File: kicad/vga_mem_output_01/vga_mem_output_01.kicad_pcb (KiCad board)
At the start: 2 copper layers, 51.3 x 26.4 mm, 18 parts, among them J1 Conn_01x03_Socket, J2 Conn_01x02_Socket, J3 Conn_01x08_Socket, U1 74LS08, U2 74LS08

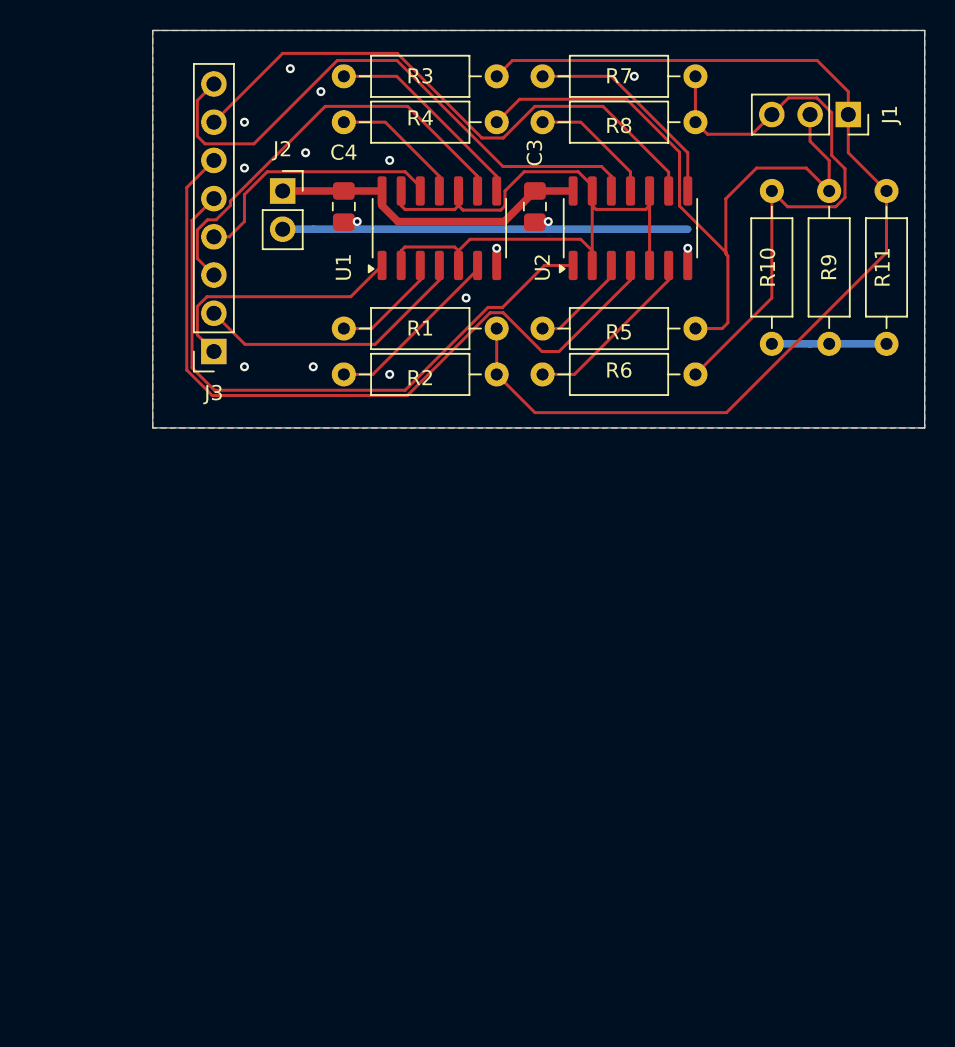
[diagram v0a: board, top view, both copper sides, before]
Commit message: more routing on 2 layer version (abandon for 4 layer version)
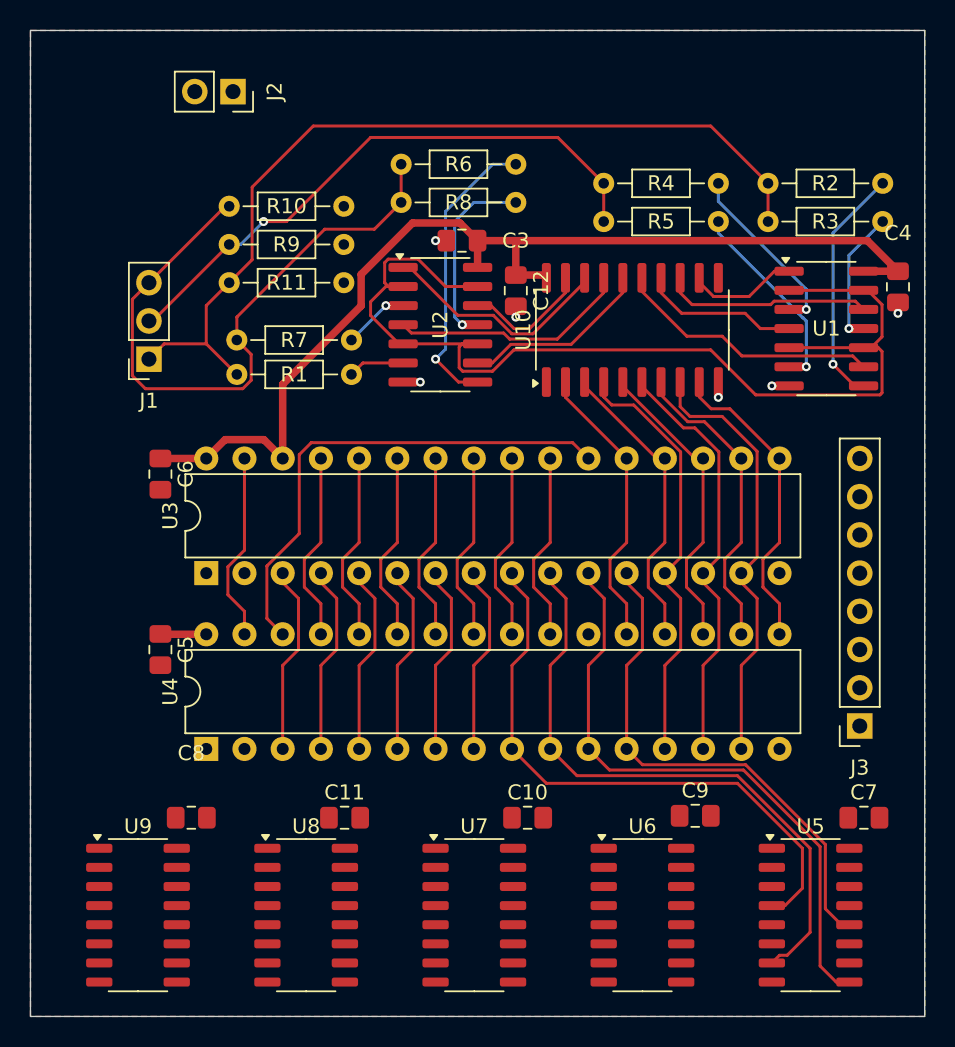
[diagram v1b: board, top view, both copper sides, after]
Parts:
- added C10: 100nF, Capacitor_SMD:C_0805_2012Metric_Pad1.18x1.45mm_HandSolder, F.Cu at (98.6, 95.0)
- added C11: 100nF, Capacitor_SMD:C_0805_2012Metric_Pad1.18x1.45mm_HandSolder, F.Cu at (86.4, 95.0)
- added C12: 100nF, Capacitor_SMD:C_0805_2012Metric_Pad1.18x1.45mm_HandSolder, F.Cu at (97.8, 60.0)
- added C5: 100nF, Capacitor_SMD:C_0805_2012Metric_Pad1.18x1.45mm_HandSolder, F.Cu at (74.2, 83.8)
- added C6: 100nF, Capacitor_SMD:C_0805_2012Metric_Pad1.18x1.45mm_HandSolder, F.Cu at (74.2, 72.2)
- added C7: 100nF, Capacitor_SMD:C_0805_2012Metric_Pad1.18x1.45mm_HandSolder, F.Cu at (120.9, 95.0)
- added C8: 100nF, Capacitor_SMD:C_0805_2012Metric_Pad1.18x1.45mm_HandSolder, F.Cu at (76.2, 95.0)
- added C9: 100nF, Capacitor_SMD:C_0805_2012Metric_Pad1.18x1.45mm_HandSolder, F.Cu at (109.7, 94.9)
- added U10: 74HCT574, Package_SO:SO-20_5.3x12.6mm_P1.27mm, F.Cu at (105.5, 62.6)
- added U3: UM61512, Package_DIP:DIP-32_W7.62mm, F.Cu at (77.2, 78.7)
- added U4: UM61512, Package_DIP:DIP-32_W7.62mm, F.Cu at (77.2, 90.4)
- added U5: 74LS157, Package_SO:SO-16_3.9x9.9mm_P1.27mm, F.Cu at (117.4, 101.5)
- added U6: 74LS157, Package_SO:SO-16_3.9x9.9mm_P1.27mm, F.Cu at (106.2, 101.5)
- added U7: 74LS157, Package_SO:SO-16_3.9x9.9mm_P1.27mm, F.Cu at (95.0, 101.5)
- added U8: 74LS157, Package_SO:SO-16_3.9x9.9mm_P1.27mm, F.Cu at (83.9, 101.5)
- added U9: 74LS157, Package_SO:SO-16_3.9x9.9mm_P1.27mm, F.Cu at (72.7, 101.5)
- R1, R10, R11, R2, R3, R4, R5, R6, R7, R8, R9: footprint Resistor_THT:R_Axial_DIN0207_L6.3mm_D2.5mm_P10.16mm_Horizontal -> Resistor_THT:R_Axial_DIN0204_L3.6mm_D1.6mm_P7.62mm_Horizontal
- moved J3 49.6 mm to (120.7, 88.9)
- moved J1 49.2 mm to (73.4, 64.5), turned to 180 degrees
- moved R2 38.0 mm to (122.2, 52.8), turned to 180 degrees
- moved C4 37.2 mm to (123.2, 59.7)
- moved R3 37.1 mm to (122.2, 55.4), turned to 180 degrees
- moved R11 36.3 mm to (86.4, 59.4), turned to 180 degrees
- moved R9 32.9 mm to (86.4, 56.9), turned to 180 degrees
- moved R10 29.9 mm to (86.4, 54.4), turned to 180 degrees
- moved U1 26.6 mm to (118.4, 62.5), turned to 0 degrees
- moved R4 25.2 mm to (111.3, 52.8), turned to 180 degrees
- moved R7 21.6 mm to (86.9, 63.2), turned to 180 degrees
- moved U2 14.2 mm to (92.8, 62.2), turned to 0 degrees
- moved R6 14.1 mm to (97.8, 51.6), turned to 180 degrees
- moved R5 13.7 mm to (111.3, 55.4), turned to 180 degrees
- moved J2 7.38 mm to (79.0, 46.7), turned to -90 degrees
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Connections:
- U1 pad 1: /PD_0 -> /PDB_3
- U1 pad 11: Net-(R4-Pad1) -> Net-(R3-Pad1)
- U1 pad 12: /PD_3 -> /PDB_2
- U1 pad 3: Net-(R1-Pad1) -> Net-(R4-Pad1)
- U1 pad 4: /PD_1 -> /PDB_4
- U1 pad 6: Net-(R2-Pad1) -> Net-(R5-Pad1)
- U1 pad 8: Net-(R3-Pad1) -> Net-(R2-Pad1)
- U1 pad 9: /PD_2 -> /PDB_1
- U2 pad 1: /PD_4 -> /PDB_6
- U2 pad 12: /PD_7 -> /PDB_7
- U2 pad 3: Net-(R5-Pad1) -> Net-(R7-Pad1)
- U2 pad 4: /PD_5 -> /PDB_0
- U2 pad 6: Net-(R6-Pad1) -> Net-(R1-Pad1)
- U2 pad 8: Net-(R7-Pad1) -> Net-(R6-Pad1)
- U2 pad 9: /PD_6 -> /PDB_5
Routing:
- net VCC: track 21.6 -> 73.5 mm
- net /A2: track 0.00 -> 41.5 mm
- net /A1: track 0.00 -> 41.0 mm
- net /A3: track 0.00 -> 39.8 mm
- net /A0: track 0.00 -> 34.7 mm
- net GND: track 38.6 -> 4.74 mm, vias 15 -> 6
- net /A16: track 0.00 -> 33.2 mm
- net /PD_5: track 51.2 -> 20.2 mm
- net /VA_EN: track 49.7 -> 73.1 mm
- net /PD_4: track 41.2 -> 20.5 mm
- net /PD_7: track 38.1 -> 19.4 mm
- net /PD_6: track 38.4 -> 20.2 mm
- net /PDB_1: track 0.00 -> 17.7 mm
- net /PDB_0: track 0.00 -> 16.0 mm
- net /PDB_6: track 0.00 -> 15.6 mm
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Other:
- board size 51.3 x 26.4 mm -> 59.4 x 65.5 mm
